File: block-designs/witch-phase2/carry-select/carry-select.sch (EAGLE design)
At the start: 11 parts, among them IC1 74LVC1G18DBVR, IC2 74AHC1G32DBV, IC3 74LVC1G08DBV

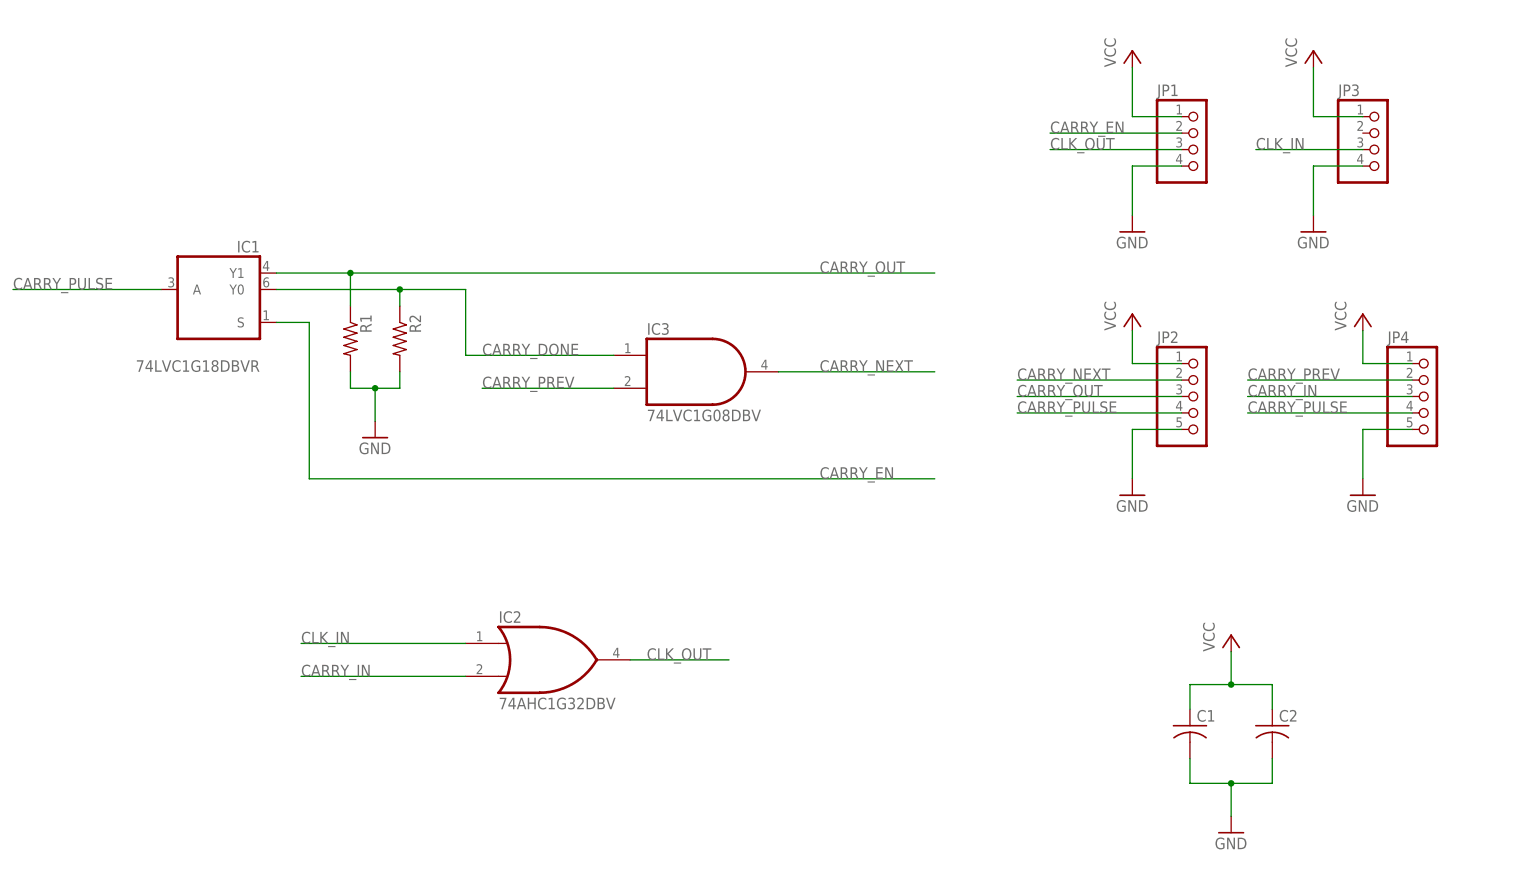
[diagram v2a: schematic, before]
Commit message: updated layout with additional caps and change to 0603 passives
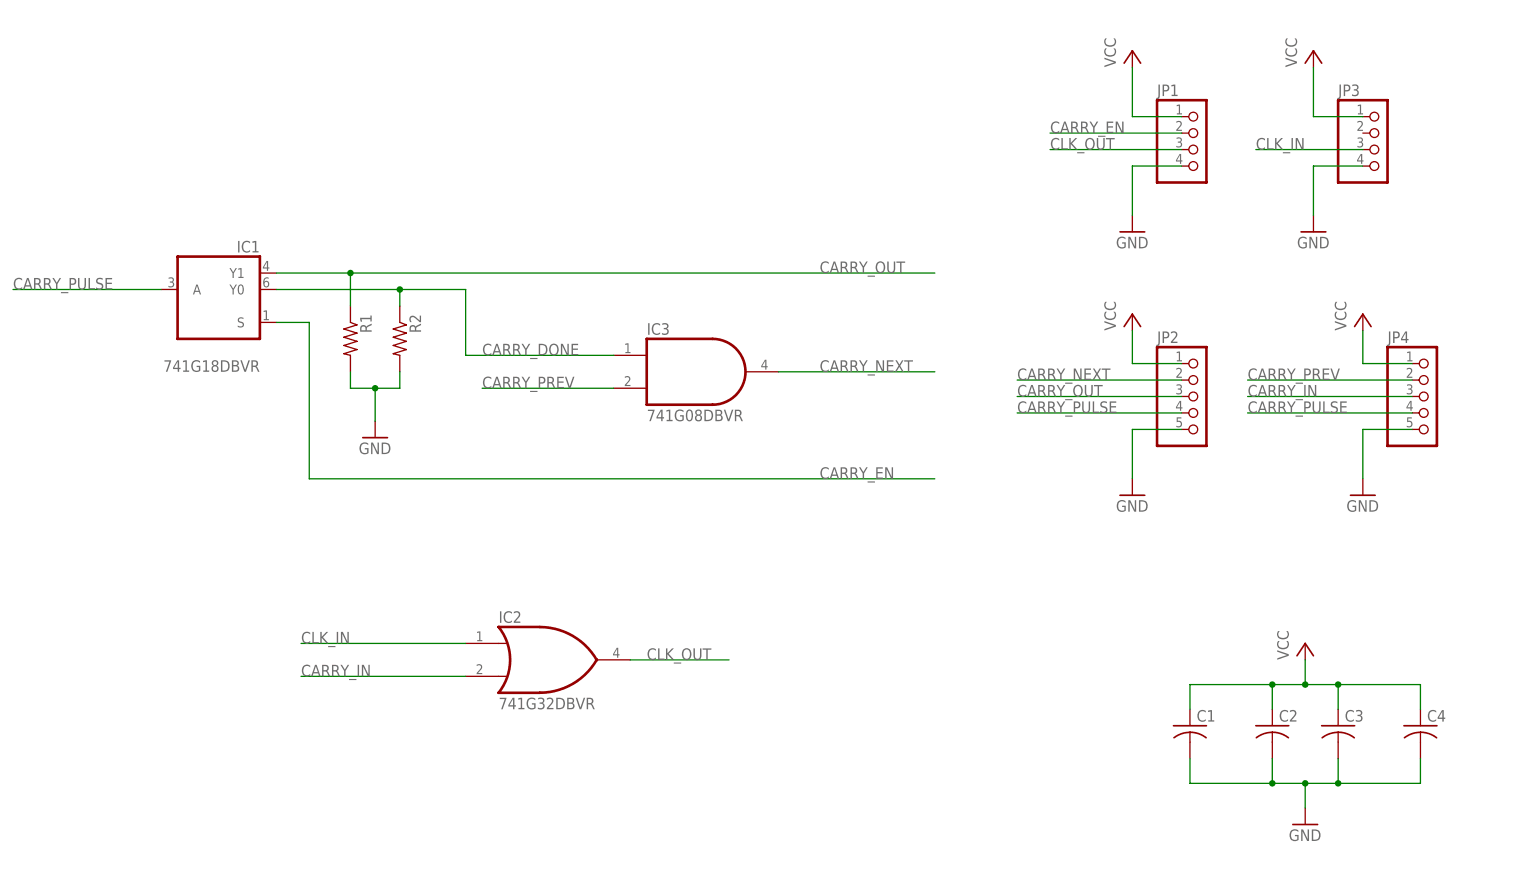
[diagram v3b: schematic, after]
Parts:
- added C3, C4: (no value), resistor:C-USC0603K
- C1, C2: device resistor:C-USC0805 -> resistor:C-USC0603K
- IC1: value 74LVC1G18DBVR -> 741G18DBVR
- IC2: value 74AHC1G32DBV -> 741G32DBVR
- IC3: value 74LVC1G08DBV -> 741G08DBVR
- R1, R2: device resistor:R-US_R0805 -> resistor:R-US_R0603
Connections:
- net GND: now also C3.2, C4.2
- net VCC: now also C3.1, C4.1

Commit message: add schmitt trigger to clock output
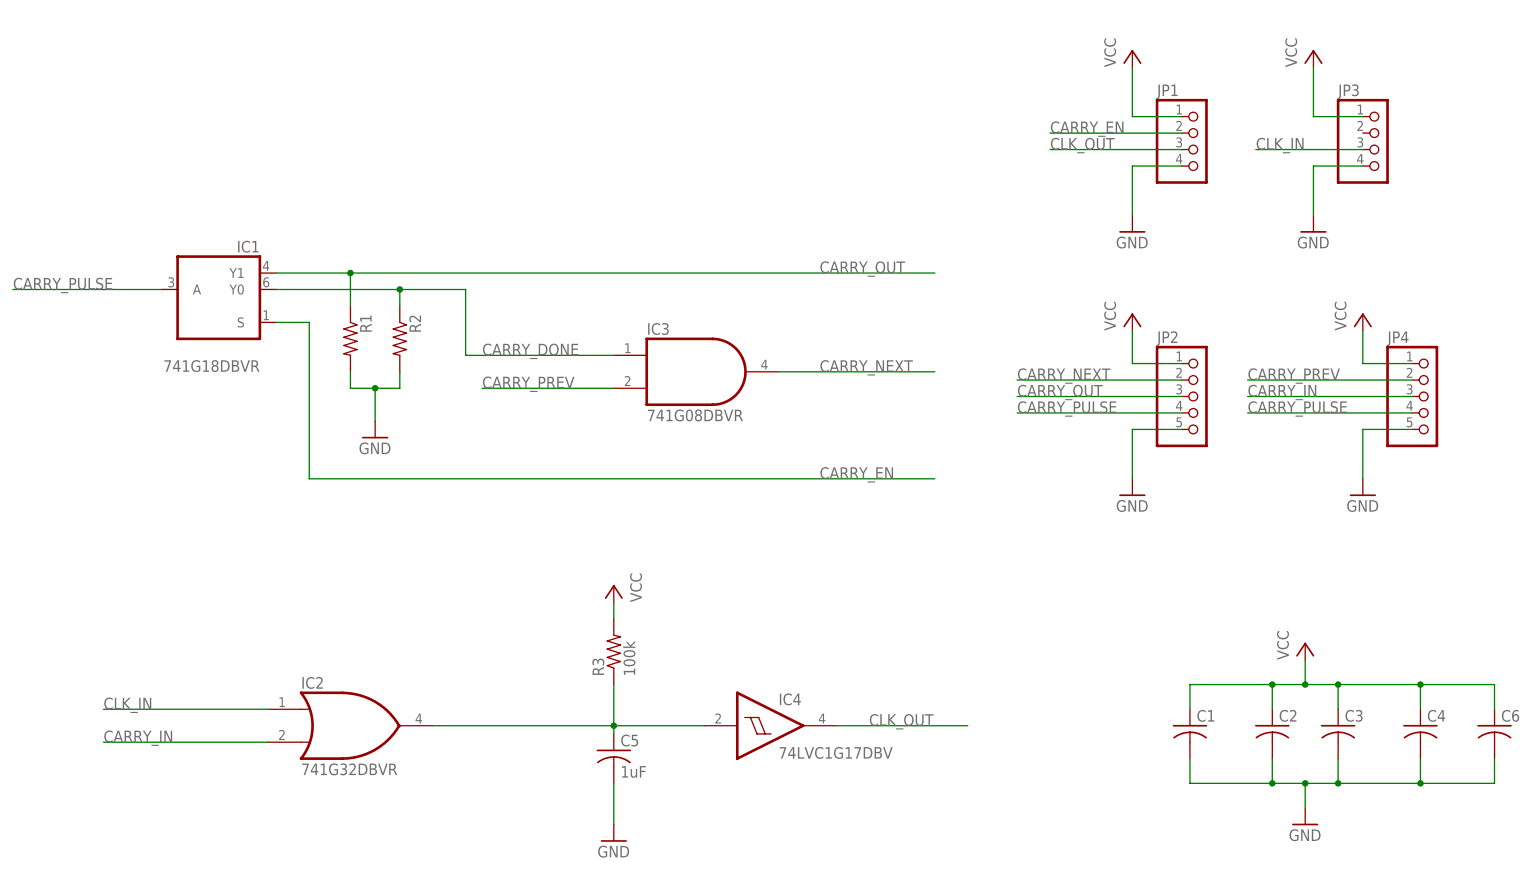
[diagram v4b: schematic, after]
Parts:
- added C5: 1uF, resistor:C-USC0603K
- added C6: (no value), resistor:C-USC0603K
- added IC4: 74LVC1G17DBV, 74xx-little-us:74LVC1G17DBV
- added R3: 100k, resistor:R-US_R0603
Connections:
- new net PRE_CLK: C5.1, IC2A.O, IC4A.I, R3.1
- net CLK_OUT: now also IC4A.O; no longer IC2A.O
- net GND: now also C5.2, C6.2
- net VCC: now also C6.1, R3.2
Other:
- moved on the sheet: IC2
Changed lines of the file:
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@@
 <layer number="132" name="bAdjust" color="7" fill="1" visible="no" active="yes"/>
 <layer number="144" name="Drill_legend" color="7" fill="1" visible="yes" active="yes"/>
+<layer number="145" name="DrillLegend_01-16" color="2" fill="9" visible="yes" active="yes"/>
 <layer number="150" name="Notes" color="7" fill="1" visible="no" active="yes"/>
 <layer number="151" name="HeatSink" color="7" fill="1" visible="yes" active="yes"/>
@@
 <layer number="230" name="230bmp" color="7" fill="1" visible="no" active="yes"/>
 <layer number="231" name="231bmp" color="7" fill="1" visible="no" active="yes"/>
+<layer number="232" name="Eagle3D_PG2" color="7" fill="1" visible="no" active="no"/>
+<layer number="233" name="Eagle3D_PG3" color="7" fill="1" visible="no" active="no"/>
 <layer number="248" name="Housing" color="7" fill="1" visible="no" active="yes"/>
 <layer number="249" name="Edge" color="7" fill="1" visible="no" active="yes"/>
@@
 <part name="C3" library="resistor" deviceset="C-US" device="C0603K"/>
 <part name="C4" library="resistor" deviceset="C-US" device="C0603K"/>
+<part name="C5" library="resistor" deviceset="C-US" device="C0603K" value="1uF"/>
+<part name="GND7" library="supply1" deviceset="GND" device=""/>
+<part name="P+7" library="supply1" deviceset="VCC" device=""/>
+<part name="R3" library="resistor" deviceset="R-US_" device="R0603" value="100k"/>
+<part name="IC4" library="74xx-little-us" deviceset="74*1G17" device="DBV" technology="LVC"/>
+<part name="C6" library="resistor" deviceset="C-US" device="C0603K"/>
 </parts>
 <sheets>
@@
 <instance part="P+5" gate="VCC" x="214.63" y="135.89"/>
 <instance part="P+2" gate="VCC" x="179.07" y="135.89"/>
-<instance part="IC2" gate="A" x="88.9" y="82.55"/>
+<instance part="IC2" gate="A" x="58.42" y="72.39"/>
 <instance part="IC3" gate="A" x="111.76" y="127"/>
 <instance part="C3" gate="G$1" x="210.82" y="72.39"/>
 <instance part="C4" gate="G$1" x="223.52" y="72.39"/>
+<instance part="C5" gate="G$1" x="99.06" y="68.58"/>
+<instance part="GND7" gate="1" x="99.06" y="54.61"/>
+<instance part="P+7" gate="VCC" x="99.06" y="93.98" rot="MR0"/>
+<instance part="R3" gate="G$1" x="99.06" y="83.82" rot="R90"/>
+<instance part="IC4" gate="A" x="123.19" y="72.39"/>
+<instance part="C6" gate="G$1" x="234.95" y="72.39"/>
 </instances>
 <busses>
@@
 <wire x1="205.74" y1="59.69" x2="205.74" y2="63.5" width="0.1524" layer="91"/>
 <junction x="205.74" y="63.5"/>
+<pinref part="C6" gate="G$1" pin="2"/>
+<wire x1="223.52" y1="63.5" x2="234.95" y2="63.5" width="0.1524" layer="91"/>
+<wire x1="234.95" y1="63.5" x2="234.95" y2="67.31" width="0.1524" layer="91"/>
+<junction x="223.52" y="63.5"/>
+</segment>
+<segment>
+<pinref part="C5" gate="G$1" pin="2"/>
+<pinref part="GND7" gate="1" pin="GND"/>
+<wire x1="99.06" y1="63.5" x2="99.06" y2="57.15" width="0.1524" layer="91"/>
 </segment>
 </net>
@@
 <wire x1="205.74" y1="82.55" x2="205.74" y2="78.74" width="0.1524" layer="91"/>
 <junction x="205.74" y="78.74"/>
+<pinref part="C6" gate="G$1" pin="1"/>
+<wire x1="223.52" y1="78.74" x2="234.95" y2="78.74" width="0.1524" layer="91"/>
+<wire x1="234.95" y1="78.74" x2="234.95" y2="74.93" width="0.1524" layer="91"/>
+<junction x="223.52" y="78.74"/>
+</segment>
+<segment>
+<pinref part="R3" gate="G$1" pin="2"/>
+<pinref part="P+7" gate="VCC" pin="VCC"/>
+<wire x1="99.06" y1="88.9" x2="99.06" y2="91.44" width="0.1524" layer="91"/>
 </segment>
 </net>
@@
 <segment>
 <pinref part="IC2" gate="A" pin="I0"/>
-<wire x1="76.2" y1="85.09" x2="50.8" y2="85.09" width="0.1524" layer="91"/>
-<label x="50.8" y="85.09" size="1.778" layer="95"/>
+<wire x1="45.72" y1="74.93" x2="20.32" y2="74.93" width="0.1524" layer="91"/>
+<label x="20.32" y="74.93" size="1.778" layer="95"/>
 </segment>
 </net>
@@
 </segment>
 <segment>
-<pinref part="IC2" gate="A" pin="O"/>
-<wire x1="101.6" y1="82.55" x2="116.84" y2="82.55" width="0.1524" layer="91"/>
-<label x="104.14" y="82.55" size="1.778" layer="95"/>
+<wire x1="133.35" y1="72.39" x2="153.67" y2="72.39" width="0.1524" layer="91"/>
+<pinref part="IC4" gate="A" pin="O"/>
+<label x="138.43" y="72.39" size="1.778" layer="95"/>
 </segment>
 </net>
@@
 <segment>
 <pinref part="IC2" gate="A" pin="I1"/>
-<wire x1="76.2" y1="80.01" x2="50.8" y2="80.01" width="0.1524" layer="91"/>
-<label x="50.8" y="80.01" size="1.778" layer="95"/>
+<wire x1="45.72" y1="69.85" x2="20.32" y2="69.85" width="0.1524" layer="91"/>
+<label x="20.32" y="69.85" size="1.778" layer="95"/>
 </segment>
 <segment>
@@
 </segment>
 </net>
+<net name="PRE_CLK" class="0">
+<segment>
+<pinref part="C5" gate="G$1" pin="1"/>
+<wire x1="99.06" y1="72.39" x2="113.03" y2="72.39" width="0.1524" layer="91"/>
+<wire x1="99.06" y1="71.12" x2="99.06" y2="72.39" width="0.1524" layer="91"/>
+<pinref part="IC4" gate="A" pin="I"/>
+<pinref part="R3" gate="G$1" pin="1"/>
+<wire x1="99.06" y1="72.39" x2="99.06" y2="78.74" width="0.1524" layer="91"/>
+<junction x="99.06" y="72.39"/>
+<pinref part="IC2" gate="A" pin="O"/>
+<wire x1="71.12" y1="72.39" x2="99.06" y2="72.39" width="0.1524" layer="91"/>
+</segment>
+</net>

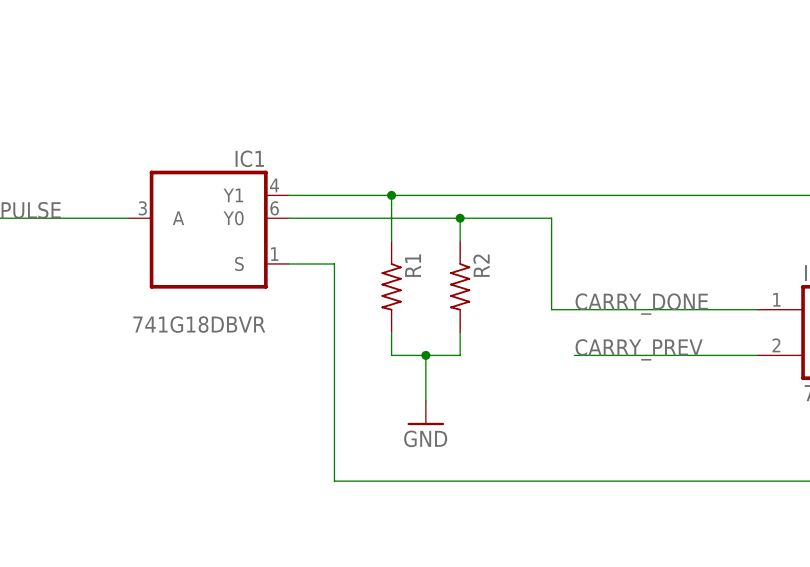
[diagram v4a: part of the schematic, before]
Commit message: add resistor values
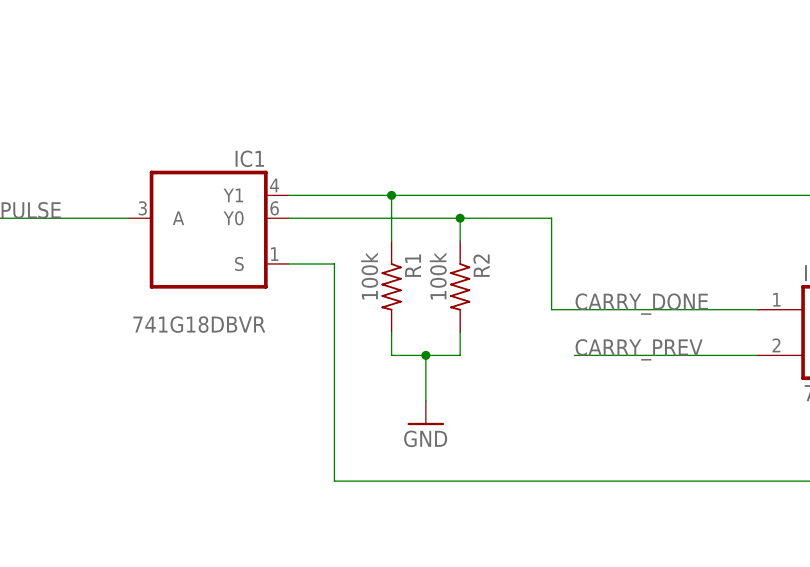
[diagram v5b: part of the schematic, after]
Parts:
- R1, R2: value (none) -> 100k
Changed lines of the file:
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@@
 <part name="P+1" library="supply1" deviceset="VCC" device=""/>
 <part name="P+4" library="supply1" deviceset="VCC" device=""/>
-<part name="R1" library="resistor" deviceset="R-US_" device="R0603"/>
-<part name="R2" library="resistor" deviceset="R-US_" device="R0603"/>
+<part name="R1" library="resistor" deviceset="R-US_" device="R0603" value="100k"/>
+<part name="R2" library="resistor" deviceset="R-US_" device="R0603" value="100k"/>
 <part name="GND1" library="supply1" deviceset="GND" device=""/>
 <part name="P+5" library="supply1" deviceset="VCC" device=""/>
